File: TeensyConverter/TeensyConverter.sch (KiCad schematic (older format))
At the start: 2 parts

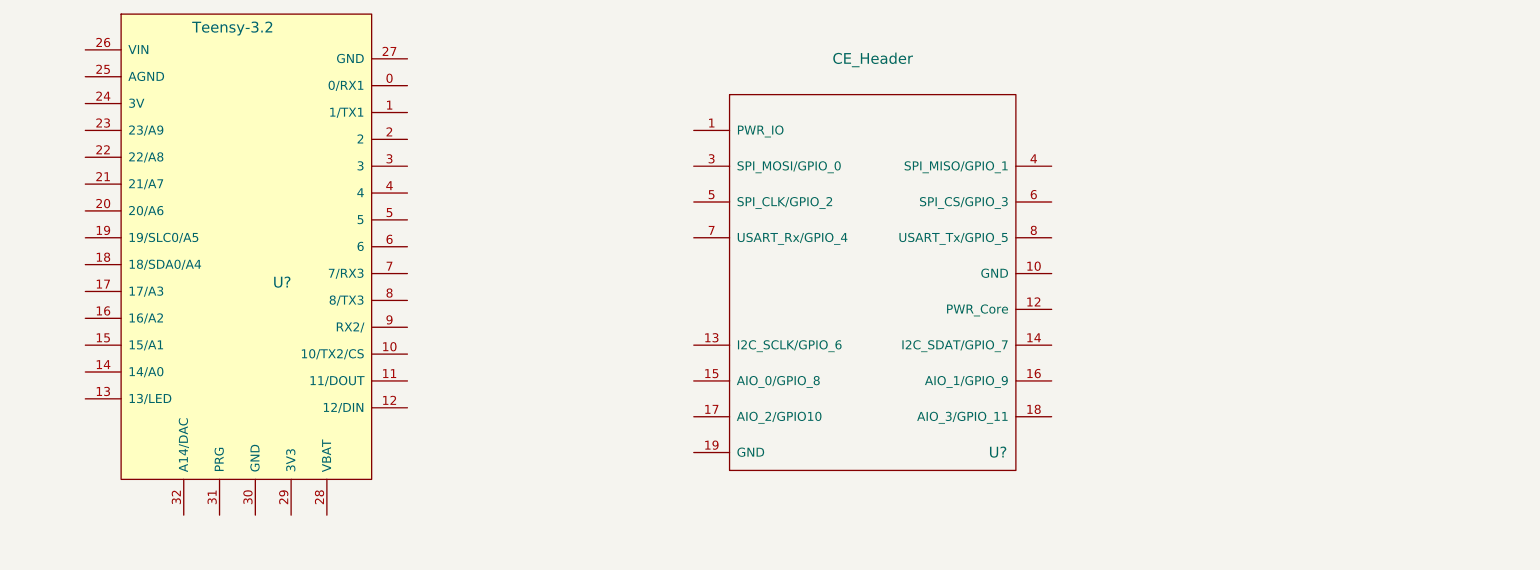
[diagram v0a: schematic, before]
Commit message: Some corrections to the symbol
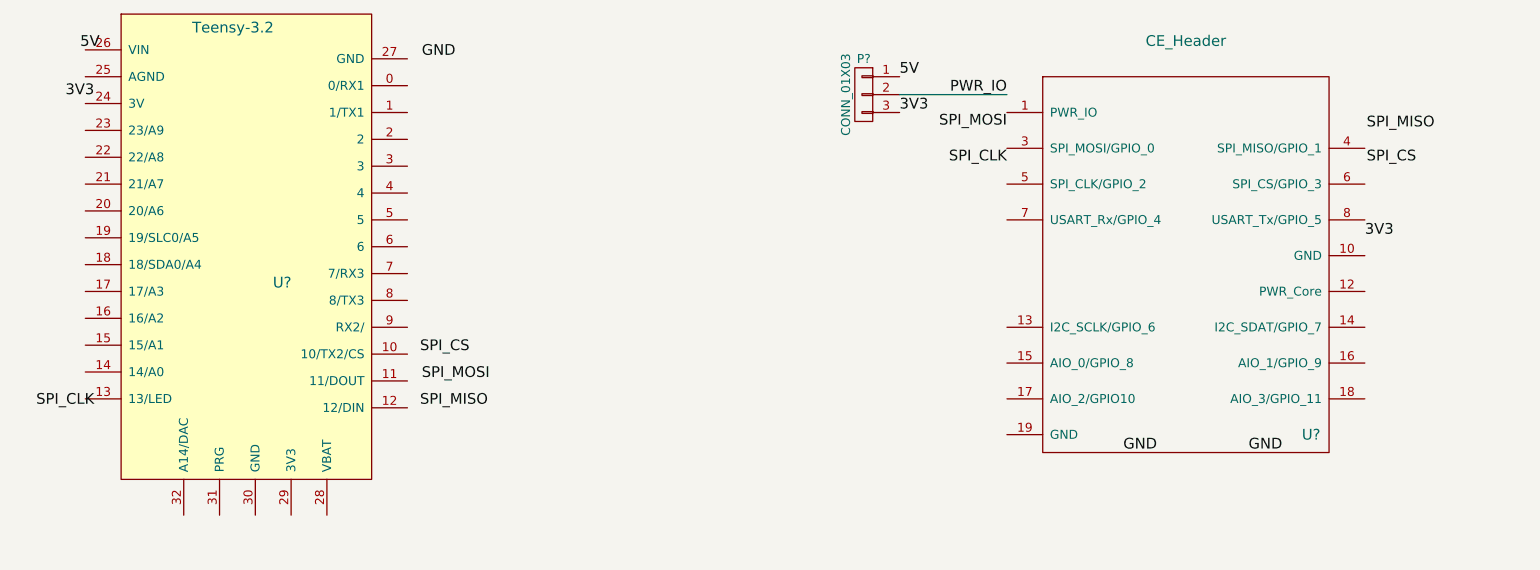
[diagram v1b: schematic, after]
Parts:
- added P?: CONN_01X03, symbol CONN_01X03
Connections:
- new net 3V3: P?.3 (P3)
- new net 5V: P?.1 (P1)
- new net PWR_IO: P?.2 (P2)
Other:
- moved on the sheet: U?
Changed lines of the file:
@@
 L CE_Header U?
 U 1 1 58C41582
-P 6500 3550
-F 0 "U?" H 7200 2550 60  0000 C CNN
-F 1 "CE_Header" H 6500 4750 60  0000 C CNN
-F 2 "" H 6100 4050 60  0000 C CNN
-F 3 "" H 6100 4050 60  0000 C CNN
-	1    6500 3550
+P 8250 3450
+F 0 "U?" H 8950 2450 60  0000 C CNN
+F 1 "CE_Header" H 8250 4650 60  0000 C CNN
+F 2 "" H 7850 3950 60  0000 C CNN
+F 3 "" H 7850 3950 60  0000 C CNN
+	1    8250 3450
 	1    0    0    -1
 $EndComp
+Text Label 7250 2550 2    60   ~ 0
+PWR_IO
+$Comp
+L CONN_01X03 P?
+U 1 1 58C417C7
+P 6450 2550
+F 0 "P?" H 6450 2750 50  0000 C CNN
+F 1 "CONN_01X03" V 6550 2550 50  0000 C CNN
+F 2 "" H 6450 2550 60  0000 C CNN
+F 3 "" H 6450 2550 60  0000 C CNN
+	1    6450 2550
+	-1   0    0    -1
+$EndComp
+Wire Wire Line
+	7250 2550 6650 2550
+Text Label 9250 3350 0    60   ~ 0
+3V3
+Text Label 6650 2650 0    60   ~ 0
+3V3
+Text Label 6650 2450 0    60   ~ 0
+5V
+Text Label 2150 2570 2    60   ~ 0
+3V3
+Text Label 2180 2300 2    60   ~ 0
+5V
+Text Label 7900 4550 0    60   ~ 0
+GND
+Text Label 8600 4550 0    60   ~ 0
+GND
+Text Label 3980 2350 0    60   ~ 0
+GND
+Text Label 7250 2740 2    60   ~ 0
+SPI_MOSI
+Text Label 3980 4150 0    60   ~ 0
+SPI_MOSI
+Text Label 7250 2940 2    60   ~ 0
+SPI_CLK
+Text Label 2150 4300 2    60   ~ 0
+SPI_CLK
+Text Label 9260 2750 0    60   ~ 0
+SPI_MISO
+Text Label 3970 4300 0    60   ~ 0
+SPI_MISO
+Text Label 9260 2940 0    60   ~ 0
+SPI_CS
+Text Label 3970 4000 0    60   ~ 0
+SPI_CS
 $EndSCHEMATC

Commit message: CE Header associated with the Teensy and the layout started
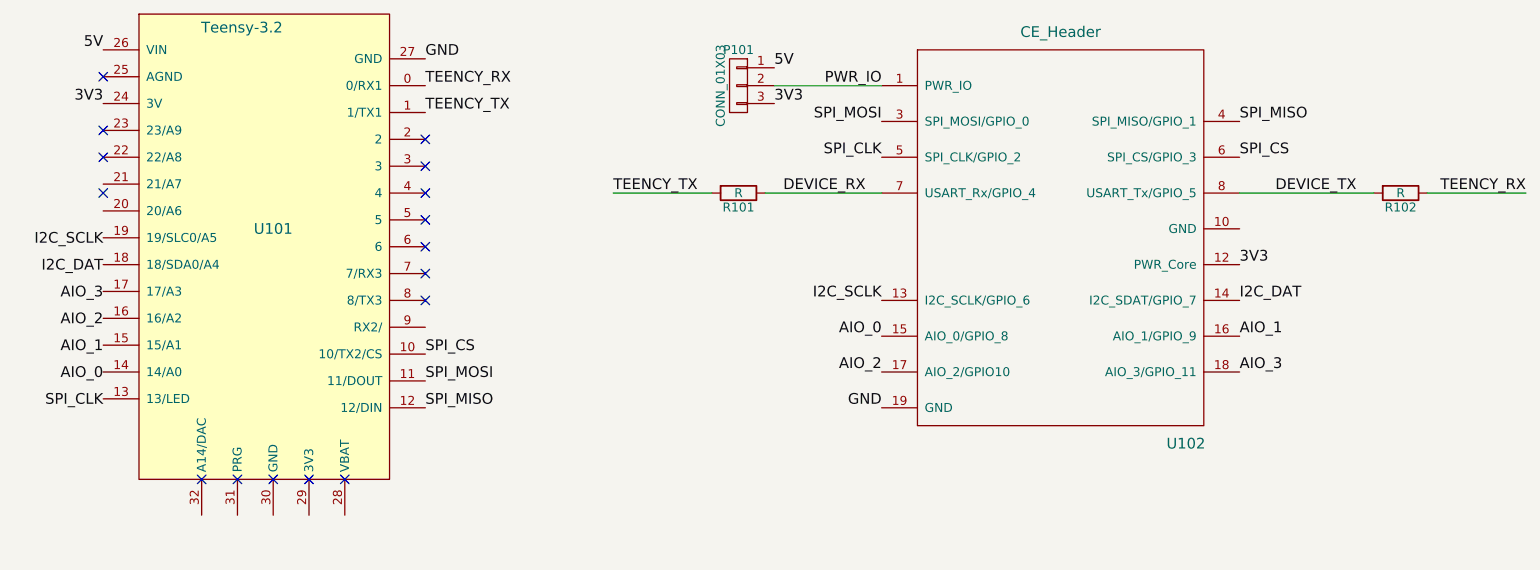
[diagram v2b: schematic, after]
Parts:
- removed U?: Teensy-3.2, symbol Teensy-3.2
- removed U?: CE_Header, symbol CE_Header
- added R101, R102: R, Resistors_SMD:R_0805_HandSoldering, symbol R
- added U101: Teensy-3.2, TeencyConverter:Teensy-32, symbol Teensy-3.2
- added U102: CE_Header, TeencyConverter:CE_Header, symbol CE_Header
- P101: renamed from P?; footprint (none) -> Pin_Headers:Pin_Header_Straight_1x03_Pitch2.54mm
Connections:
- net 3V3: now also U101.24 (3V), U102.12 (PWR_Core)
- net 5V: now also U101.26 (VIN)
- net GND: now also U101.27 (GND), U102.19 (GND)
- net PWR_IO: now also U102.1 (PWR_IO)
- net SPI_CLK: now also U102.5 (SPI_CLK/GPIO_2)
- net SPI_CS: now also U101.10 (10/TX2/CS), U102.6 (SPI_CS/GPIO_3)
- net SPI_MISO: now also U101.12 (12/DIN), U102.4 (SPI_MISO/GPIO_1)
- net SPI_MOSI: now also U101.11 (11/DOUT), U102.3 (SPI_MOSI/GPIO_0)
- new net AIO_0: U102.15 (AIO_0/GPIO_8)
- new net AIO_1: U102.16 (AIO_1/GPIO_9)
- new net AIO_2: U102.17 (AIO_2/GPIO10)
- new net AIO_3: U102.18 (AIO_3/GPIO_11)
- new net DEVICE_RX: R101.1, U102.7 (USART_Rx/GPIO_4)
- new net DEVICE_TX: R102.2, U102.8 (USART_Tx/GPIO_5)
- new net I2C_DAT: U102.14 (I2C_SDAT/GPIO_7)
- new net I2C_SCLK: U102.13 (I2C_SCLK/GPIO_6)
- new net TEENCY_RX: R102.1, U101.0 (0/RX1)
- new net TEENCY_TX: R101.2, U101.1 (1/TX1)
- no-connect marks 0 -> 16
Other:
- moved on the sheet: P101
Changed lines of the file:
@@
 EESchema Schematic File Version 2
+LIBS:TeensyConverter-rescue
 LIBS:ce_header
 LIBS:teensy-32
@@
 Comment4 ""
 $EndDescr
+Text Label 6550 2500 2    60   ~ 0
+PWR_IO
 $Comp
-L Teensy-3.2 U?
-U 1 1 58C4153D
-P 3050 3350
-F 0 "U?" H 3200 3100 60  0000 C CNN
-F 1 "Teensy-3.2" H 2925 4525 60  0000 C CNN
-F 2 "" H 2825 3025 60  0001 C CNN
-F 3 "" H 2825 3025 60  0001 C CNN
-	1    3050 3350
+L CONN_01X03 P101
+U 1 1 58C417C7
+P 5750 2500
+F 0 "P101" H 5750 2700 50  0000 C CNN
+F 1 "CONN_01X03" V 5850 2500 50  0000 C CNN
+F 2 "Pin_Headers:Pin_Header_Straight_1x03_Pitch2.54mm" H 5750 2500 60  0001 C CNN
+F 3 "" H 5750 2500 60  0000 C CNN
+	1    5750 2500
+	-1   0    0    -1
+$EndComp
+Wire Wire Line
+	6550 2500 5950 2500
+Text Label 8550 3500 0    60   ~ 0
+3V3
+Text Label 5950 2600 0    60   ~ 0
+3V3
+Text Label 5950 2400 0    60   ~ 0
+5V
+Text Label 2200 2600 2    60   ~ 0
+3V3
+Text Label 2200 2300 2    60   ~ 0
+5V
+Text Label 4000 2350 0    60   ~ 0
+GND
+Text Label 6550 2700 2    60   ~ 0
+SPI_MOSI
+Text Label 4000 4150 0    60   ~ 0
+SPI_MOSI
+Text Label 6550 2900 2    60   ~ 0
+SPI_CLK
+Text Label 2200 4300 2    60   ~ 0
+SPI_CLK
+Text Label 8550 2700 0    60   ~ 0
+SPI_MISO
+Text Label 4000 4300 0    60   ~ 0
+SPI_MISO
+Text Label 8550 2900 0    60   ~ 0
+SPI_CS
+Text Label 4000 4000 0    60   ~ 0
+SPI_CS
+$Comp
+L CE_Header U102
+U 1 1 58D750A7
+P 7550 3300
+F 0 "U102" H 8250 2100 60  0000 C CNN
+F 1 "CE_Header" H 7550 4400 60  0000 C CNN
+F 2 "TeencyConverter:CE_Header" H 7150 3700 60  0001 C CNN
+F 3 "" H 7150 3700 60  0000 C CNN
+	1    7550 3300
 	1    0    0    -1
 $EndComp
 $Comp
-L CE_Header U?
-U 1 1 58C41582
-P 8250 3450
-F 0 "U?" H 8950 2450 60  0000 C CNN
-F 1 "CE_Header" H 8250 4650 60  0000 C CNN
-F 2 "" H 7850 3950 60  0000 C CNN
-F 3 "" H 7850 3950 60  0000 C CNN
-	1    8250 3450
+L Teensy-3.2 U101
+U 1 1 58D756B3
+P 3150 3350
+F 0 "U101" H 3150 3400 60  0000 C CNN
+F 1 "Teensy-3.2" H 2975 4525 60  0000 C CNN
+F 2 "TeencyConverter:Teensy-32" H 2875 3025 60  0001 C CNN
+F 3 "" H 2875 3025 60  0001 C CNN
+	1    3150 3350
 	1    0    0    -1
 $EndComp
-Text Label 7250 2550 2    60   ~ 0
-PWR_IO
 $Comp
-L CONN_01X03 P?
-U 1 1 58C417C7
-P 6450 2550
-F 0 "P?" H 6450 2750 50  0000 C CNN
-F 1 "CONN_01X03" V 6550 2550 50  0000 C CNN
-F 2 "" H 6450 2550 60  0000 C CNN
-F 3 "" H 6450 2550 60  0000 C CNN
-	1    6450 2550
-	-1   0    0    -1
+L R R101
+U 1 1 58D8069B
+P 5750 3100
+F 0 "R101" V 5830 3100 50  0000 C CNN
+F 1 "R" V 5750 3100 50  0000 C CNN
+F 2 "Resistors_SMD:R_0805_HandSoldering" V 5680 3100 30  0001 C CNN
+F 3 "" H 5750 3100 30  0000 C CNN
+	1    5750 3100
+	0    1    1    0
+$EndComp
+$Comp
+L R R102
+U 1 1 58D80714
+P 9450 3100
+F 0 "R102" V 9530 3100 50  0000 C CNN
+F 1 "R" V 9450 3100 50  0000 C CNN
+F 2 "Resistors_SMD:R_0805_HandSoldering" V 9380 3100 30  0001 C CNN
+F 3 "" H 9450 3100 30  0000 C CNN
+	1    9450 3100
+	0    1    1    0
 $EndComp
 Wire Wire Line
-	7250 2550 6650 2550
-Text Label 9250 3350 0    60   ~ 0
-3V3
-Text Label 6650 2650 0    60   ~ 0
-3V3
-Text Label 6650 2450 0    60   ~ 0
-5V
-Text Label 2150 2570 2    60   ~ 0
-3V3
-Text Label 2180 2300 2    60   ~ 0
-5V
-Text Label 7900 4550 0    60   ~ 0
+	6550 3100 5900 3100
+Wire Wire Line
+	8550 3100 9300 3100
+Text Label 8750 3100 0    60   ~ 0
+DEVICE_TX
+Text Label 10150 3100 2    60   ~ 0
+TEENCY_RX
+Text Label 6000 3100 0    60   ~ 0
+DEVICE_RX
+Text Label 5050 3100 0    60   ~ 0
+TEENCY_TX
+Text Label 4000 2650 0    60   ~ 0
+TEENCY_TX
+Text Label 4000 2500 0    60   ~ 0
+TEENCY_RX
+Text Label 6550 3700 2    60   ~ 0
+I2C_SCLK
+Text Label 2200 3400 2    60   ~ 0
+I2C_SCLK
+Text Label 8550 3700 0    60   ~ 0
+I2C_DAT
+Text Label 2200 3550 2    60   ~ 0
+I2C_DAT
+Text Label 6550 3900 2    60   ~ 0
+AIO_0
+Text Label 2200 4150 2    60   ~ 0
+AIO_0
+Text Label 8550 3900 0    60   ~ 0
+AIO_1
+Text Label 2200 4000 2    60   ~ 0
+AIO_1
+Text Label 2200 3850 2    60   ~ 0
+AIO_2
+Text Label 2200 3700 2    60   ~ 0
+AIO_3
+Text Label 6550 4100 2    60   ~ 0
+AIO_2
+Text Label 8550 4100 0    60   ~ 0
+AIO_3
+Wire Wire Line
+	5600 3100 5050 3100
+Wire Wire Line
+	9600 3100 10150 3100
+NoConn ~ 4000 2800
+NoConn ~ 4000 2950
+NoConn ~ 4000 3100
+NoConn ~ 4000 3250
+NoConn ~ 4000 3400
+NoConn ~ 4000 3550
+NoConn ~ 4000 3700
+NoConn ~ 3550 4700
+NoConn ~ 3350 4700
+NoConn ~ 3150 4700
+NoConn ~ 2950 4700
+NoConn ~ 2750 4700
+NoConn ~ 2200 2450
+NoConn ~ 2200 2750
+NoConn ~ 2200 2900
+NoConn ~ 2200 3100
+Text Label 6550 4300 2    60   ~ 0
 GND
-Text Label 8600 4550 0    60   ~ 0
-GND
-Text Label 3980 2350 0    60   ~ 0
-GND
-Text Label 7250 2740 2    60   ~ 0
-SPI_MOSI
-Text Label 3980 4150 0    60   ~ 0
-SPI_MOSI
-Text Label 7250 2940 2    60   ~ 0
-SPI_CLK
-Text Label 2150 4300 2    60   ~ 0
-SPI_CLK
-Text Label 9260 2750 0    60   ~ 0
-SPI_MISO
-Text Label 3970 4300 0    60   ~ 0
-SPI_MISO
-Text Label 9260 2940 0    60   ~ 0
-SPI_CS
-Text Label 3970 4000 0    60   ~ 0
-SPI_CS
 $EndSCHEMATC

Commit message: Created the layout and submitted to OSH Park
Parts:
- removed U101: Teensy-3.2, TeencyConverter:Teensy-32, symbol Teensy-3.2
- removed U102: CE_Header, TeencyConverter:CE_Header, symbol CE_Header
- added H1: CE_Header, CE_Header:CE_Header, symbol CE_Header
- added U1: Teensy-3.2, TeencyConverter:Teensy-32, symbol Teensy-3.2
- P1: renamed from P101; footprint Pin_Headers:Pin_Header_Straight_1x03_Pitch2.54mm -> TeencyConverter:Pin_Header_Straight_1x03_Pitch2.54mm
- renumbered R101 to R1, R102 to R2
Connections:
- net 3V3: now also H1.12 (PWR_Core), U1.24 (3V)
- net 5V: now also U1.26 (VIN)
- net AIO_0: now also H1.15 (AIO_0/GPIO_8), U1.14 (14/A0)
- net AIO_1: now also H1.16 (AIO_1/GPIO_9), U1.15 (15/A1)
- net AIO_2: now also H1.17 (AIO_2/GPIO10), U1.16 (16/A2)
- net AIO_3: now also H1.18 (AIO_3/GPIO_11), U1.17 (17/A3)
- net DEVICE_RX: now also H1.7 (USART_Rx/GPIO_4)
- net DEVICE_TX: now also H1.8 (USART_Tx/GPIO_5)
- net GND: now also H1.10 (GND), H1.19 (GND), U1.27 (GND), U1.30 (GND)
- net I2C_DAT: now also H1.14 (I2C_SDAT/GPIO_7), U1.18 (18/SDA0/A4)
- net I2C_SCLK: now also H1.13 (I2C_SCLK/GPIO_6), U1.19 (19/SLC0/A5)
- net PWR_IO: now also H1.1 (PWR_IO)
- net SPI_CLK: now also H1.5 (SPI_CLK/GPIO_2), U1.13 (13/LED)
- net SPI_CS: now also H1.6 (SPI_CS/GPIO_3), U1.10 (10/TX2/CS)
- net SPI_MISO: now also H1.4 (SPI_MISO/GPIO_1), U1.12 (12/DIN)
- net SPI_MOSI: now also H1.3 (SPI_MOSI/GPIO_0), U1.11 (11/DOUT)
- net TEENCY_RX: now also U1.0 (0/RX1)
- net TEENCY_TX: now also U1.1 (1/TX1)
- no-connect marks 16 -> 15
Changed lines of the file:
@@
 EESchema Schematic File Version 2
-LIBS:TeensyConverter-rescue
 LIBS:ce_header
 LIBS:teensy-32
@@
 PWR_IO
 $Comp
-L CONN_01X03 P101
+L CONN_01X03 P1
 U 1 1 58C417C7
 P 5750 2500
-F 0 "P101" H 5750 2700 50  0000 C CNN
+F 0 "P1" H 5750 2700 50  0000 C CNN
 F 1 "CONN_01X03" V 5850 2500 50  0000 C CNN
-F 2 "Pin_Headers:Pin_Header_Straight_1x03_Pitch2.54mm" H 5750 2500 60  0001 C CNN
+F 2 "TeencyConverter:Pin_Header_Straight_1x03_Pitch2.54mm" H 5750 2500 60  0001 C CNN
 F 3 "" H 5750 2500 60  0000 C CNN
 	1    5750 2500
@@
 Text Label 6550 2900 2    60   ~ 0
 SPI_CLK
-Text Label 2200 4300 2    60   ~ 0
+Text Label 2200 4250 2    60   ~ 0
 SPI_CLK
 Text Label 8550 2700 0    60   ~ 0
@@
 SPI_CS
 $Comp
-L CE_Header U102
-U 1 1 58D750A7
-P 7550 3300
-F 0 "U102" H 8250 2100 60  0000 C CNN
-F 1 "CE_Header" H 7550 4400 60  0000 C CNN
-F 2 "TeencyConverter:CE_Header" H 7150 3700 60  0001 C CNN
-F 3 "" H 7150 3700 60  0000 C CNN
-	1    7550 3300
-	1    0    0    -1
-$EndComp
-$Comp
-L Teensy-3.2 U101
-U 1 1 58D756B3
-P 3150 3350
-F 0 "U101" H 3150 3400 60  0000 C CNN
-F 1 "Teensy-3.2" H 2975 4525 60  0000 C CNN
-F 2 "TeencyConverter:Teensy-32" H 2875 3025 60  0001 C CNN
-F 3 "" H 2875 3025 60  0001 C CNN
-	1    3150 3350
-	1    0    0    -1
-$EndComp
-$Comp
-L R R101
+L R R1
 U 1 1 58D8069B
 P 5750 3100
-F 0 "R101" V 5830 3100 50  0000 C CNN
+F 0 "R1" V 5830 3100 50  0000 C CNN
 F 1 "R" V 5750 3100 50  0000 C CNN
 F 2 "Resistors_SMD:R_0805_HandSoldering" V 5680 3100 30  0001 C CNN
@@
 $EndComp
 $Comp
-L R R102
+L R R2
 U 1 1 58D80714
 P 9450 3100
-F 0 "R102" V 9530 3100 50  0000 C CNN
+F 0 "R2" V 9530 3100 50  0000 C CNN
 F 1 "R" V 9450 3100 50  0000 C CNN
 F 2 "Resistors_SMD:R_0805_HandSoldering" V 9380 3100 30  0001 C CNN
@@
 Text Label 6550 3700 2    60   ~ 0
 I2C_SCLK
-Text Label 2200 3400 2    60   ~ 0
+Text Label 2200 3350 2    60   ~ 0
 I2C_SCLK
 Text Label 8550 3700 0    60   ~ 0
 I2C_DAT
-Text Label 2200 3550 2    60   ~ 0
+Text Label 2200 3500 2    60   ~ 0
 I2C_DAT
 Text Label 6550 3900 2    60   ~ 0
 AIO_0
-Text Label 2200 4150 2    60   ~ 0
+Text Label 2200 4100 2    60   ~ 0
 AIO_0
 Text Label 8550 3900 0    60   ~ 0
 AIO_1
-Text Label 2200 4000 2    60   ~ 0
+Text Label 2200 3950 2    60   ~ 0
 AIO_1
-Text Label 2200 3850 2    60   ~ 0
+Text Label 2200 3800 2    60   ~ 0
 AIO_2
-Text Label 2200 3700 2    60   ~ 0
+Text Label 2200 3650 2    60   ~ 0
 AIO_3
 Text Label 6550 4100 2    60   ~ 0
@@
 NoConn ~ 4000 3550
 NoConn ~ 4000 3700
-NoConn ~ 3550 4700
-NoConn ~ 3350 4700
-NoConn ~ 3150 4700
-NoConn ~ 2950 4700
-NoConn ~ 2750 4700
+NoConn ~ 3550 4900
+NoConn ~ 3350 4900
+NoConn ~ 2950 4900
+NoConn ~ 2750 4900
 NoConn ~ 2200 2450
 NoConn ~ 2200 2750
 NoConn ~ 2200 2900
-NoConn ~ 2200 3100
+NoConn ~ 2200 3050
 Text Label 6550 4300 2    60   ~ 0
 GND
+$Comp
+L Teensy-3.2 U1
+U 1 1 58D95B37
+P 3150 3350
+F 0 "U1" H 3150 3400 60  0000 C CNN
+F 1 "Teensy-3.2" H 2975 4525 60  0000 C CNN
+F 2 "TeencyConverter:Teensy-32" H 2875 3025 60  0001 C CNN
+F 3 "" H 2875 3025 60  0001 C CNN
+	1    3150 3350
+	1    0    0    -1
+$EndComp
+Text Label 3150 4900 3    60   ~ 0
+GND
+$Comp
+L CE_Header H1
+U 1 1 58DA1984
+P 7550 3300
+F 0 "H1" H 8250 2100 60  0000 C CNN
+F 1 "CE_Header" H 7550 4400 60  0000 C CNN
+F 2 "CE_Header:CE_Header" H 7150 3700 60  0001 C CNN
+F 3 "" H 7150 3700 60  0000 C CNN
+	1    7550 3300
+	1    0    0    -1
+$EndComp
+Text Label 8550 3300 0    60   ~ 0
+GND
 $EndSCHEMATC
